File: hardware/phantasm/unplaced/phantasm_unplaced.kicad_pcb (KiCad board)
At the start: 4 copper layers, 58.3 x 32 mm, 29 parts, among them J1 +5V IN ~1A, J2 LED sig DI/CI/SIG_GND, J3A SYNC in, J3B SYNC out, J4 debug, U1 74AHCT125

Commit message: pcb: preserve corrected Teensy footprint orientation
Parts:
- F1: value 0.75A -> 0.5A

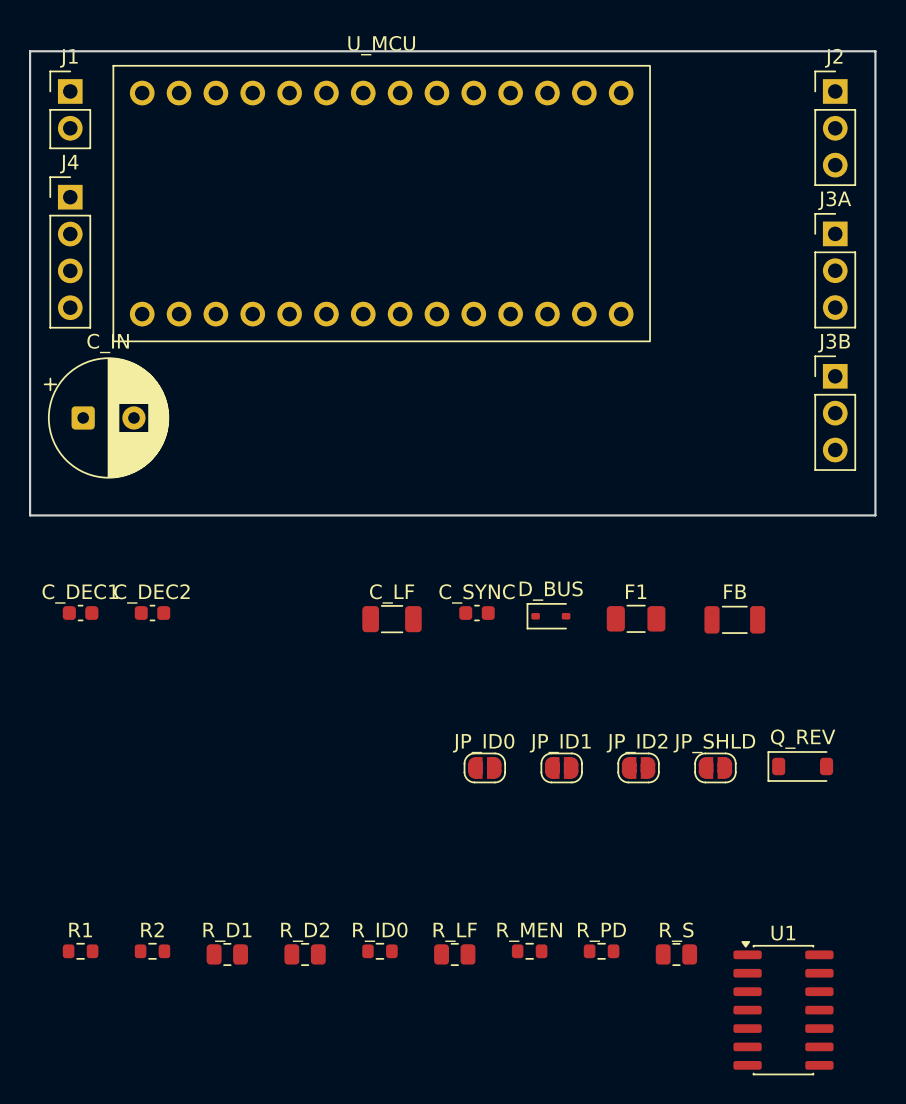
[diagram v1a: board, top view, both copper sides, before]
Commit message: pcb: constrain Quilter signal-integrity placement
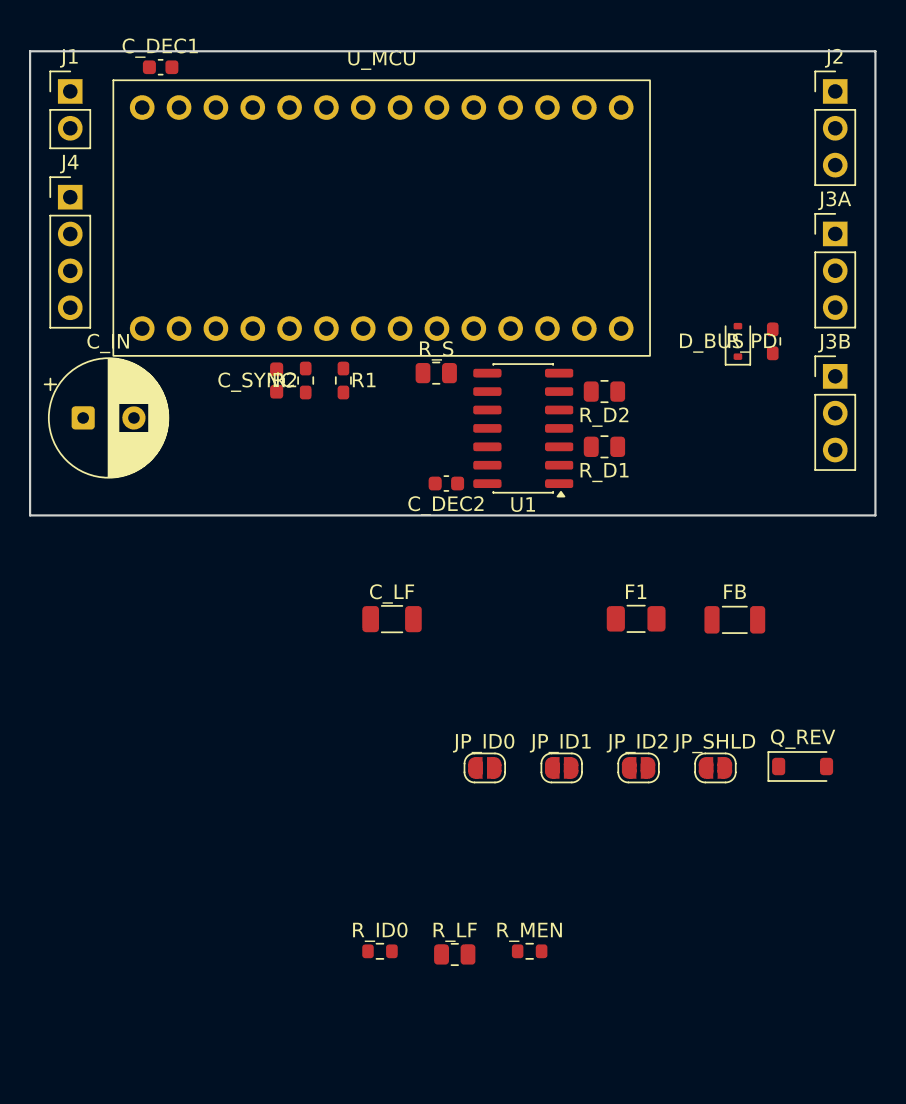
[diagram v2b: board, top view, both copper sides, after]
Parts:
- moved R_D2 44.0 mm to (39.6, 23.5), turned to 180 degrees
- moved U1 43.9 mm to (34.0, 26.0), turned to 180 degrees
- moved R_PD 43.7 mm to (51.2, 20.0), turned to 90 degrees
- moved R_D1 43.6 mm to (39.6, 27.3), turned to 180 degrees
- moved R_S 43.4 mm to (28.0, 22.2)
- moved R1 43.3 mm to (21.6, 22.7), turned to -90 degrees
- moved R2 40.7 mm to (19.0, 22.7), turned to 90 degrees
- moved C_DEC1 38.0 mm to (9.00, 1.10)
- moved D_BUS 22.9 mm to (48.8, 20.0), turned to 90 degrees
- moved C_DEC2 22.1 mm to (28.7, 29.8), turned to 180 degrees
- moved C_SYNC 21.2 mm to (17.0, 22.7), turned to 90 degrees
- moved U_MCU 1.00 mm to (24.2, 11.5)
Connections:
- net +5V_IN renamed /+5V_IN
- net +5V_PROT renamed /+5V_PROT
- net CLK renamed /CLK
- net CLK_IN renamed /CLK_IN
- net CLK_SRC renamed /CLK_SRC
- net DATA renamed /DATA
- net DATA_IN renamed /DATA_IN
- net DATA_SRC renamed /DATA_SRC
- net FRAME_SYNC renamed /FRAME_SYNC
- net ID0 renamed /ID0
- net ID1 renamed /ID1
- net ID2 renamed /ID2
- net LF_DAMP renamed /LF_DAMP
- net MASTER_EN renamed /MASTER_EN
- net SERIAL1_TX renamed /SERIAL1_TX
- net SHIELD renamed /SHIELD
- net SYNC_BUS renamed /SYNC_BUS
- net SYNC_SRC renamed /SYNC_SRC
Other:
- board text added: "PHANTASM segment board UNPLACED - 58.28x32mm outline (width <=35mm); mechanical and signal-integrity placements locked"
- board text removed: "PHANTASM segment board UNPLACED - 58.28x32mm outline (width <=35mm); THT + tall C_IN locked on TOP, SMD staged below for Quilter"

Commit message: pcb: complete PHANTASM fabrication safeguards
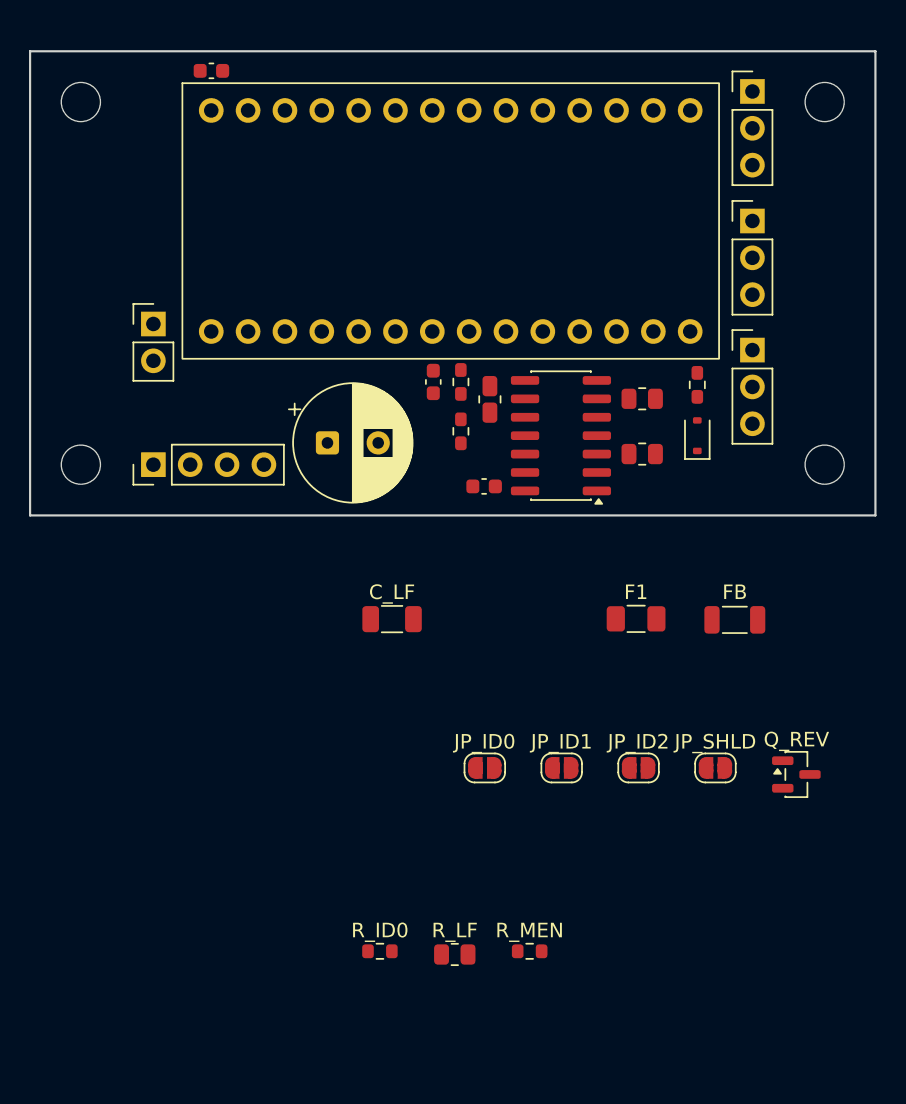
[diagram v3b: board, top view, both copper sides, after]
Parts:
- removed the Q_REV at (53.3, 49.3)
- added H1: M2.5, MountingHole:MountingHole_2.7mm_M2.5, F.Cu at (3.50, 3.50)
- added H2: M2.5, MountingHole:MountingHole_2.7mm_M2.5, F.Cu at (3.50, 28.5)
- added H3: M2.5, MountingHole:MountingHole_2.7mm_M2.5, F.Cu at (54.8, 3.50)
- added H4: M2.5, MountingHole:MountingHole_2.7mm_M2.5, F.Cu at (54.8, 28.5)
- added Q_REV: AO3401A, Package_TO_SOT_SMD:SOT-23, F.Cu at (52.8, 49.9)
- F1: value 0.5A -> 0.5A hold
- moved J4 19.3 mm to (8.50, 28.5), turned to 90 degrees
- moved J1 17.0 mm to (8.50, 18.8)
- moved C_IN 16.9 mm to (20.5, 27.0)
- moved C_SYNC 10.8 mm to (27.8, 22.8)
- moved R2 10.7 mm to (29.7, 22.8)
- moved R1 8.82 mm to (29.7, 26.2), turned to 90 degrees
- moved D_BUS 7.08 mm to (46.0, 26.5)
- moved R_PD 6.00 mm to (46.0, 23.0)
- moved J3B 5.99 mm to (49.8, 20.6)
- moved J3A 5.78 mm to (49.8, 11.7)
- moved J2 5.71 mm to (49.8, 2.77)
- moved U_MCU 4.76 mm to (29.0, 11.7)
- moved R_S 4.12 mm to (31.7, 24.0), turned to 90 degrees
- moved C_DEC1 3.51 mm to (12.5, 1.35)
- moved R_D1 2.65 mm to (42.2, 27.8)
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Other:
- board text added: "0 OPEN OPEN MASTER"
- board text added: "1 GND OPEN A-SOUTH"
- board text added: "2 OPEN GND B-NORTH"
- board text added: "3 GND GND B-SOUTH"
- board text added: "BOARD ID: ____"
- board text added: "ID ID0 ID1 ROLE"
- board text added: "MASTER = ALL ID OPEN SHLD = MASTER ONLY"
- board text added: "USB PLUG KEEP-OUT"

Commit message: PCB rev 1.1
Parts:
- removed R_ID0: 10k DNP, Resistor_SMD:R_0603_1608Metric
- D_BUS: value TVS -> CDSOD323-T05L
- moved JP_ID0 47.8 mm to (56.0, 8.50), turned to 90 degrees
- moved JP_ID1 42.2 mm to (56.0, 11.9), turned to 90 degrees
- moved JP_ID2 36.9 mm to (56.0, 15.3), turned to 90 degrees
- moved JP_SHLD 31.6 mm to (56.0, 19.0), turned to 90 degrees
- moved R_LF 4.96 mm to (24.3, 62.3)
- moved R_MEN 4.96 mm to (29.5, 62.0)
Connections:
- R_PD pad 2: GND -> /SYNC_PULLDOWN
- U1 pad 11: unconnected-(U1-Pad11) -> /SYNC_PULLDOWN
- U1 pad 13: +5V_LOGIC -> /MASTER_EN
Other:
- board text added: "G"
- board text added: "H"
- board text added: "ID0"
- board text added: "ID1"
- board text added: "ID2"
- board text added: "Phantasm Rev 1.1"
- board text added: "S"
- board text added: "SHLD"
- board text added: "SYNC IN"
- board text added: "SYNC OUT"

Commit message: pcb: restore JP_ID2 silkscreen (finding 65)
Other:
- board text added: "N8 ID2 OPEN=0-3 GND=4-7; M=OPEN; SHLD=M"
- board text removed: "MASTER = ALL ID OPEN SHLD = MASTER ONLY"
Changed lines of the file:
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@@
 		)
 	)
-	(gr_text "MASTER = ALL ID OPEN   SHLD = MASTER ONLY"
+	(gr_text "N8 ID2 OPEN=0-3 GND=4-7; M=OPEN; SHLD=M"
 		(at 29.14 17 0)
 		(layer "B.SilkS")

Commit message: hardware: raise sync TVS standoff above the drive rail (finding 317)
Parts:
- D_BUS: value CDSOD323-T05L -> CDSOD323-T08L
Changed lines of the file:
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@@
 			)
 		)
-		(property "Value" "CDSOD323-T05L"
+		(property "Value" "CDSOD323-T08L"
 			(at 0.1 1.9 0)
 			(layer "F.Fab")

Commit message: hardware: place the strip return between data and clock (finding 318)
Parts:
- J2: value LED sig DI/CI/SIG_GND -> LED sig DI/SIG_GND/CI
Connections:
- J2 pad 2: /CLK -> GND
- J2 pad 3: GND -> /CLK
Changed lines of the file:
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@@
 			)
 		)
-		(property "Value" "LED sig DI/CI/SIG_GND"
+		(property "Value" "LED sig DI/SIG_GND/CI"
 			(at 0 7.46 0)
 			(layer "F.Fab")
@@
 			(layers "*.Cu" "*.Mask")
 			(remove_unused_layers no)
-			(net "/CLK")
+			(net "GND")
 		)
 		(pad "3" thru_hole circle
@@
 			(layers "*.Cu" "*.Mask")
 			(remove_unused_layers no)
-			(net "GND")
+			(net "/CLK")
 		)
 		(embedded_fonts no)
